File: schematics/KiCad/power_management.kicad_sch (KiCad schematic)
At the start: 52 parts, among them J3 USB_C, Q1 DMG6601LVT-7, Q2 DMG6601LVT-7, Q3 DMG9926UDM, SW4 TL1105SF160R, U4 AP2112K-3.3, U5 MP2615AGQ-Z, U6 BQ29700DSER

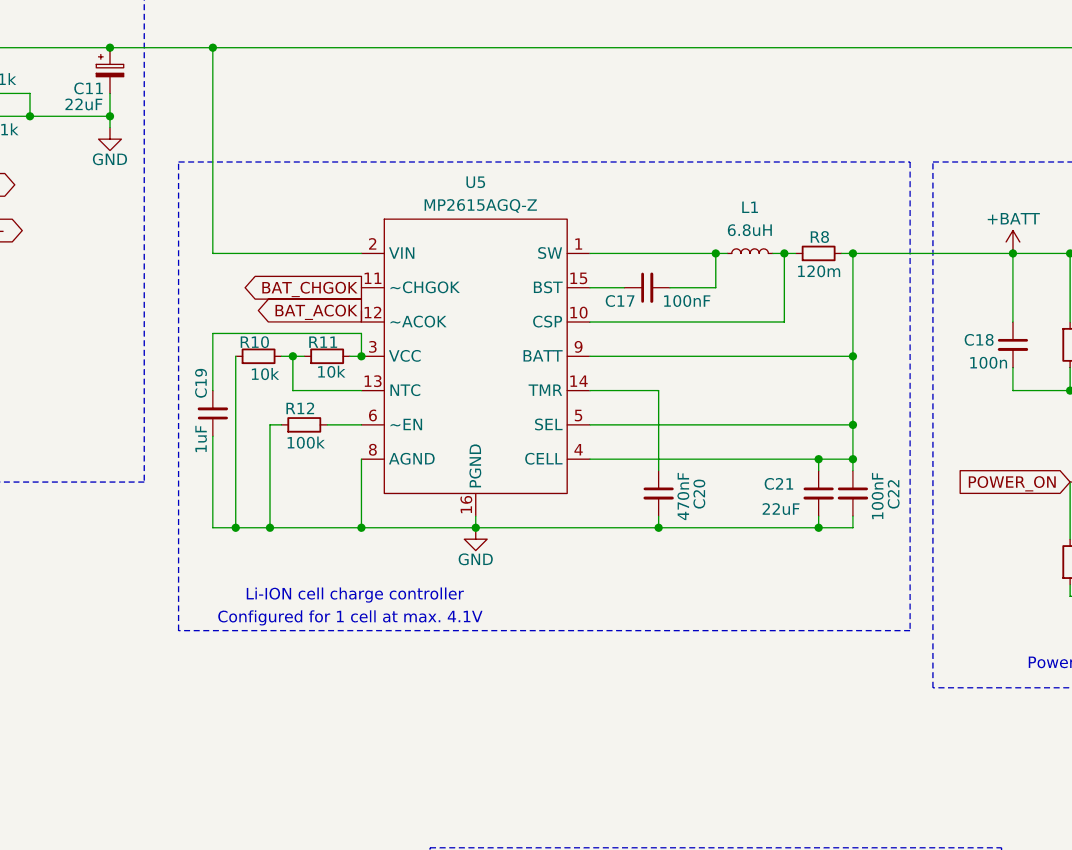
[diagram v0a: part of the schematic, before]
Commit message: re-wire cell selection pins of the charger
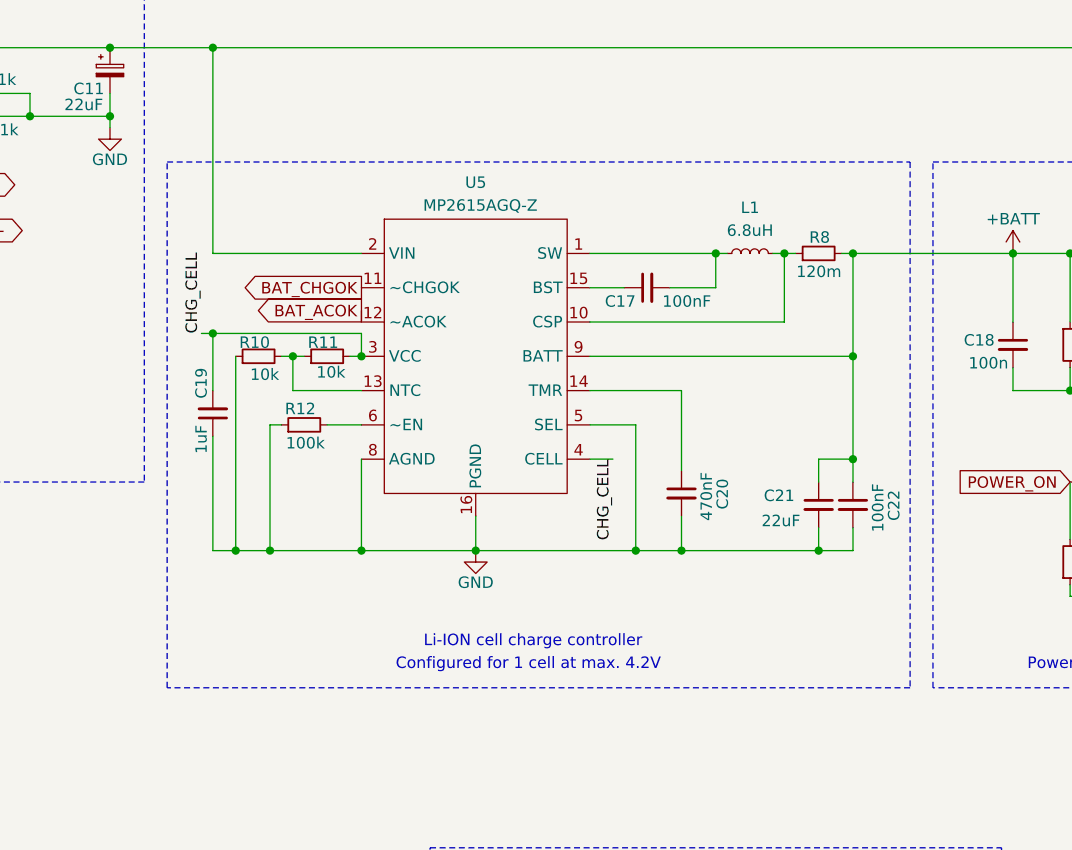
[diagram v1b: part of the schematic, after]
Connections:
- net +BATT: no longer U5.4 (CELL), U5.5 (SEL)
- net GND: now also U5.5 (SEL)
- net CHG_CELL: now reaches C19.2, R11.2, U5.3 (VCC)
- net CHG_CELL: now also U5.4 (CELL)
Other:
- note added: "Configured for 1 cell at max. 4.2V"
- note removed: "Configured for 1 cell at max. 4.1V"
- moved on the sheet: C20, C21, C22

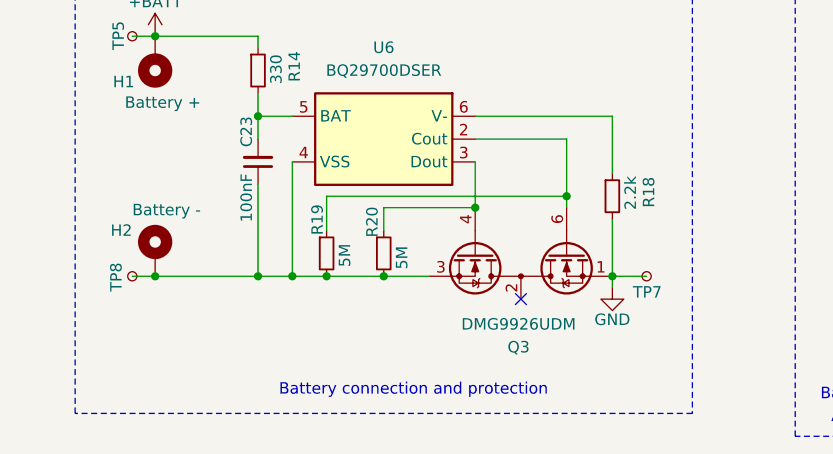
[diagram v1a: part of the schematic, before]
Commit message: re-annotate test points
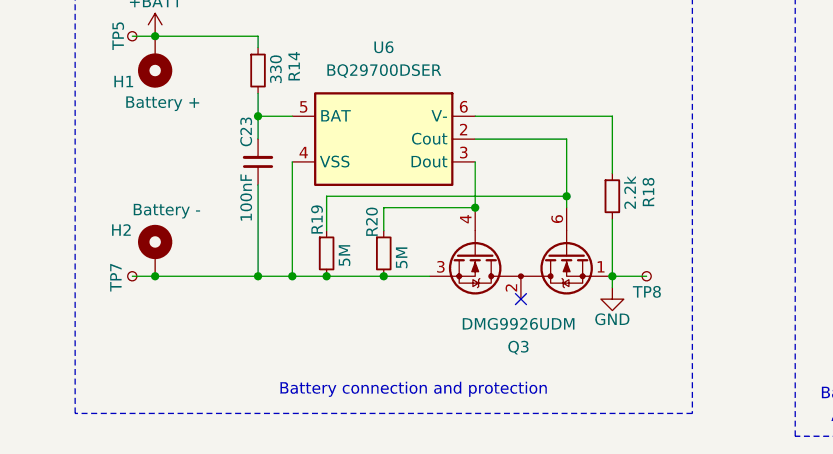
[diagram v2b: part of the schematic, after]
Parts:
- renumbered TP8 to TP7, TP7 to TP8
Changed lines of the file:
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@@
 		(on_board yes)
 		(dnp no)
-		(property "Reference" "TP7"
+		(property "Reference" "TP8"
 			(at 82.296 157.988 90)
 			(effects
@@
 			(project "leany"
 				(path "/e47b2519-93ca-4a48-9414-ecc253dd35f5/702fc064-eab2-4b82-8f62-a654ccd28f72"
-					(reference "TP7")
+					(reference "TP8")
 					(unit 1)
 				)
@@
 		(on_board yes)
 		(dnp no)
-		(property "Reference" "TP8"
+		(property "Reference" "TP7"
 			(at 24.892 154.686 90)
 			(effects
@@
 			(project "leany"
 				(path "/e47b2519-93ca-4a48-9414-ecc253dd35f5/702fc064-eab2-4b82-8f62-a654ccd28f72"
-					(reference "TP8")
-					(unit 1)
-				)
+					(reference "TP7")
+					(unit 1)
+				)

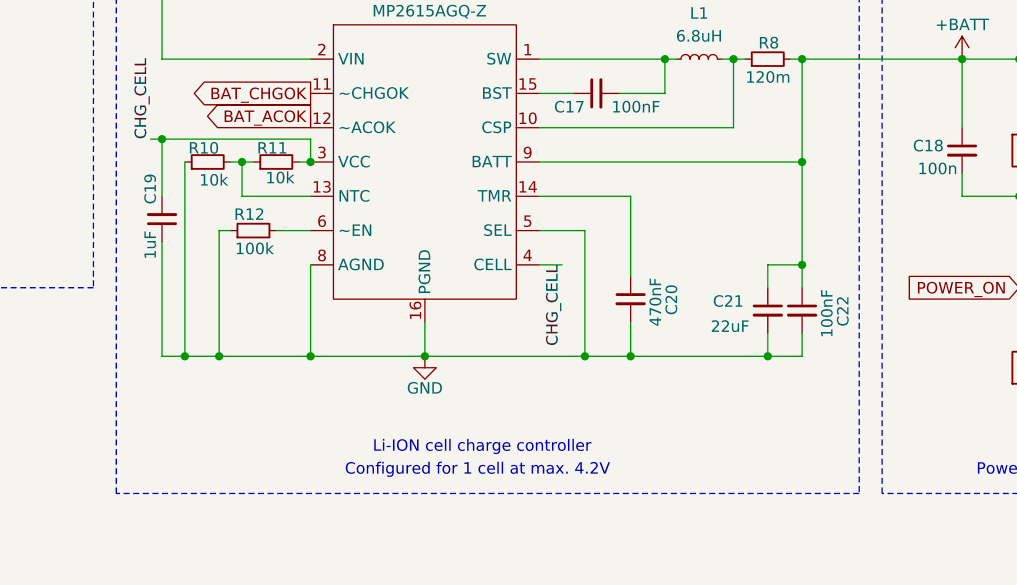
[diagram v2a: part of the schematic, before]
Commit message: change battery decoupling capacitor
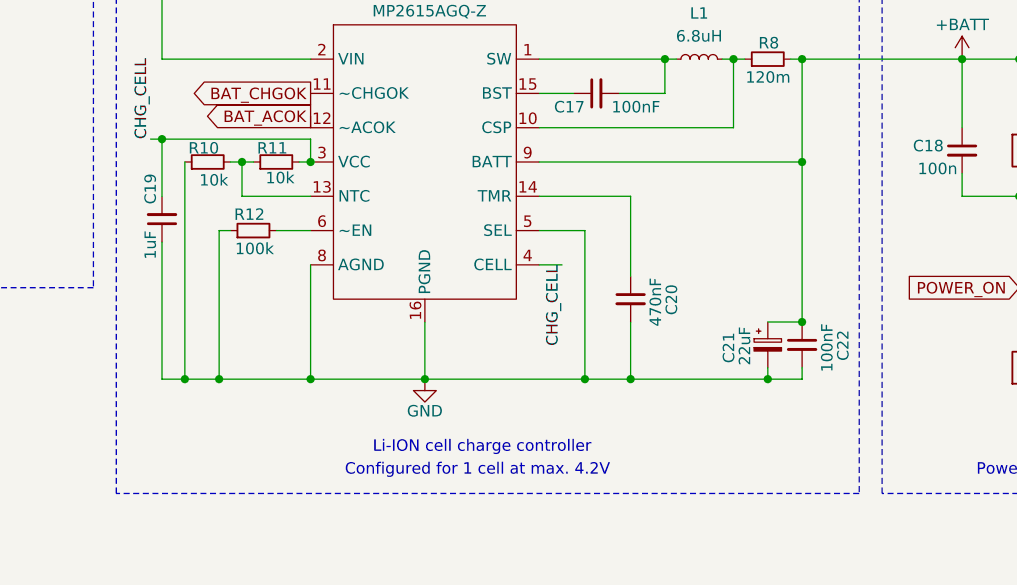
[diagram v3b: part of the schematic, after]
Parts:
- removed C21: 22uF, Capacitor_SMD:C_0201_0603Metric, symbol Device:C_Small
- added C21: 22uF, symbol Device:C_Polarized_Small
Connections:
- net +BATT: now also C21.1
- net GND: now also C21.2
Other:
- moved on the sheet: C22

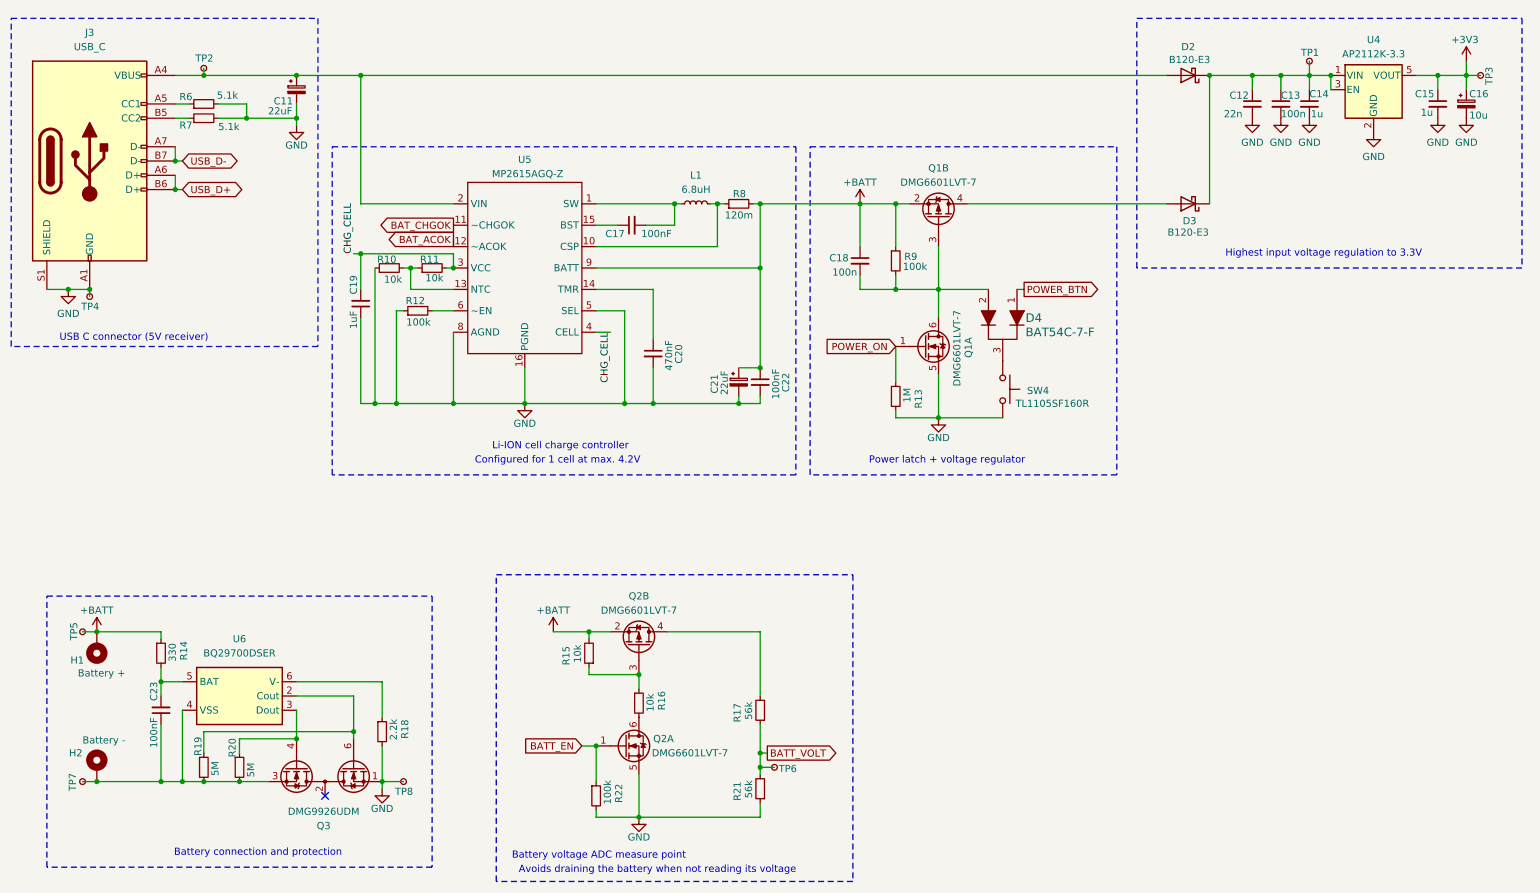
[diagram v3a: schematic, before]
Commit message: assign footprints + add an ideal diode
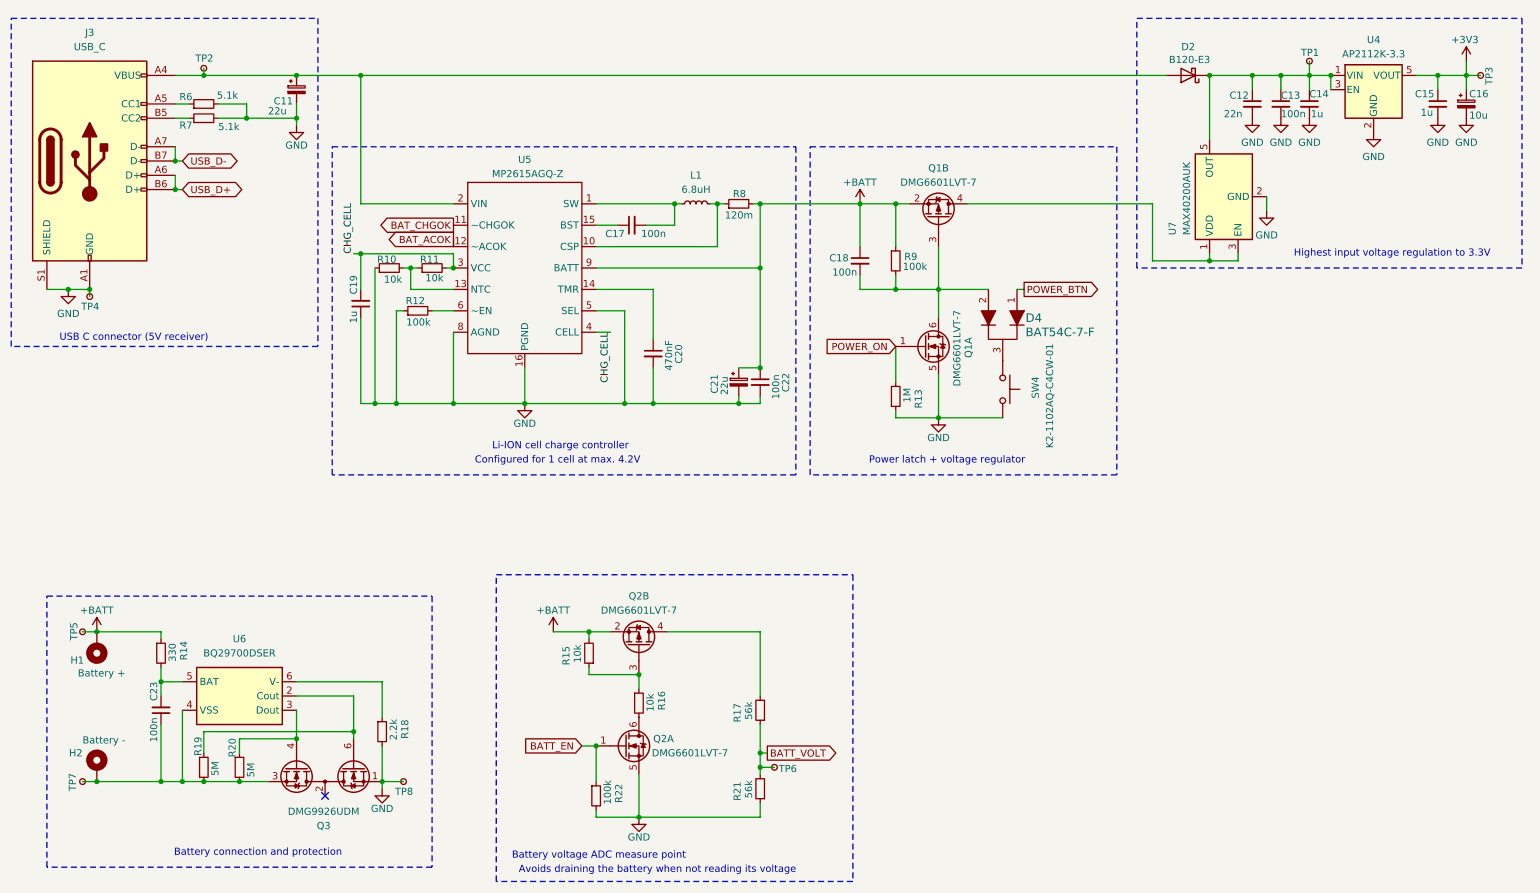
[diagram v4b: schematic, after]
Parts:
- removed D3: B120-E3, Diode_SMD:D_SMA, symbol Diode:B120-E3
- added U7: MAX40200AUK, Package_TO_SOT_SMD:SOT-23-5, symbol Analog_Switch:MAX40200AUK
- C11, C21: value 22uF -> 22u; footprint (none) -> Capacitor_SMD:C_0805_2012Metric
- C12, C13, C14, C15, C18, C20: footprint Capacitor_SMD:C_0201_0603Metric -> Capacitor_SMD:C_0603_1608Metric
- C16: footprint (none) -> Capacitor_SMD:C_0603_1608Metric
- C17, C22, C23: value 100nF -> 100n; footprint Capacitor_SMD:C_0201_0603Metric -> Capacitor_SMD:C_0603_1608Metric
- C19: value 1uF -> 1u; footprint Capacitor_SMD:C_0201_0603Metric -> Capacitor_SMD:C_0603_1608Metric
- D4: footprint digikey-footprints:SOT-23-3 -> Package_TO_SOT_SMD:SOT-23
- SW4: value TL1105SF160R -> K2-1102AQ-C4CW-01; footprint (none) -> Button_Switch_THT:SW_Tactile_SPST_Angled_PTS645Vx31-2LFS
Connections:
- net GND: now also U7.2 (GND)
- net at Q1.4 (D): now also U7.1 (VDD), U7.3 (EN)
- net at C12.1, C13.1, C14.1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: now also U7.5 (OUT)

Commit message: start using a new li-ion charger
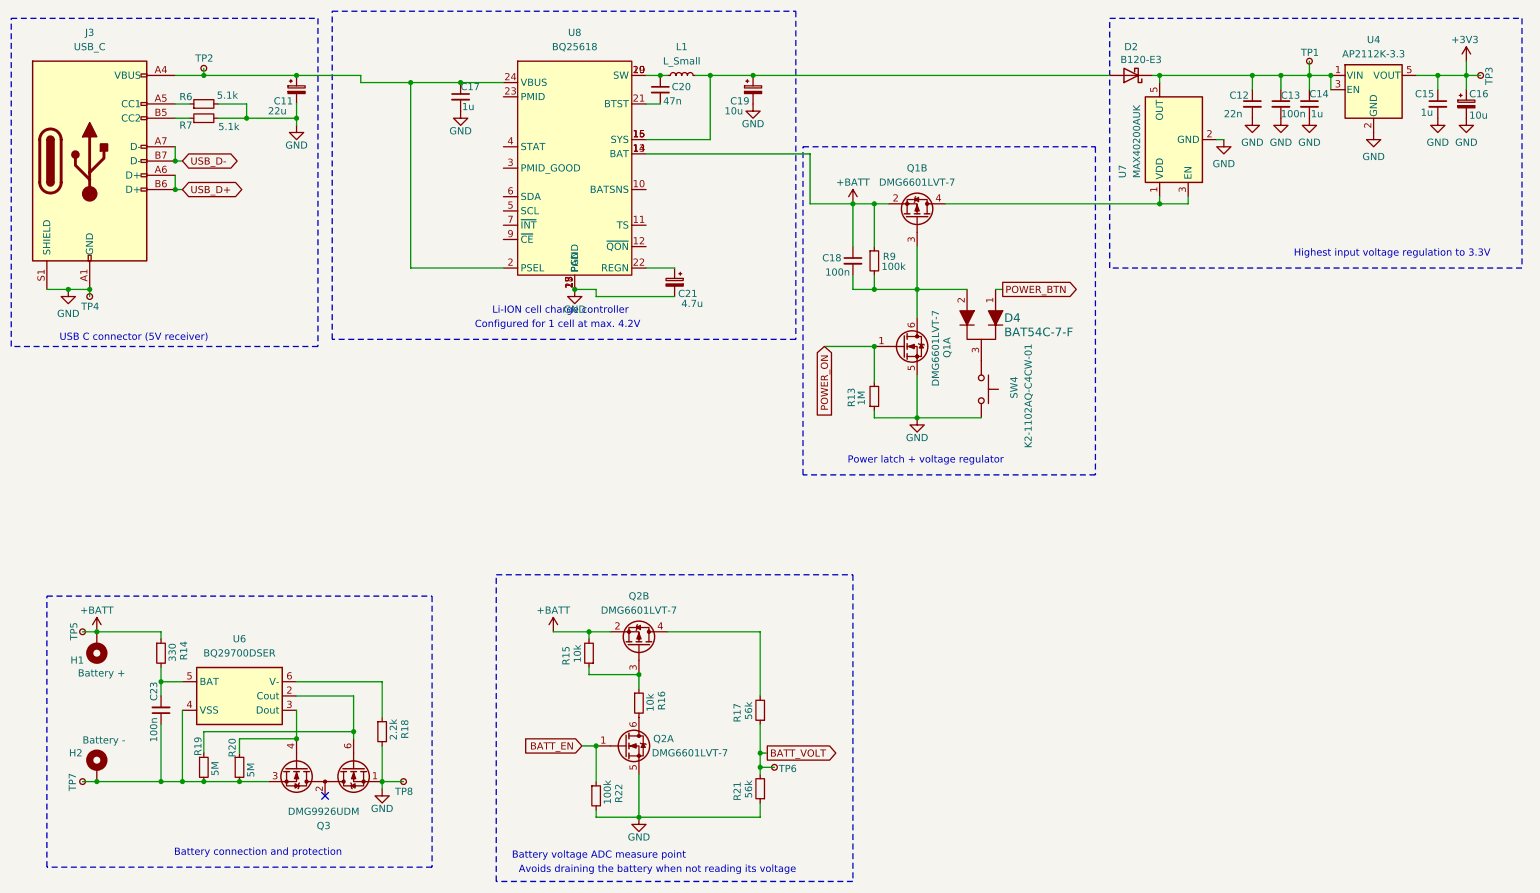
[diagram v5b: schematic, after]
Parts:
- removed C19: 1u, Capacitor_SMD:C_0603_1608Metric, symbol Device:C_Small
- removed C22: 100n, Capacitor_SMD:C_0603_1608Metric, symbol Device:C_Small
- removed R10, R11: 10k, Resistor_SMD:R_0603_1608Metric, symbol Device:R_Small
- removed R12: 100k, Resistor_SMD:R_0603_1608Metric, symbol Device:R_Small
- removed R8: 120m, Resistor_SMD:R_0603_1608Metric, symbol Device:R_Small
- removed U5: MP2615AGQ-Z, symbol leany-symbols:MP2615AGQ-Z
- added C19: 10u, Capacitor_SMD:C_0805_2012Metric, symbol Device:C_Polarized_Small
- added U8: BQ25618, Package_DFN_QFN:Texas_RGE0024H_VQFN-24-1EP_4x4mm_P0.5mm_EP2.7x2.7mm_ThermalVias, symbol leany-symbols:BQ25618
- C17: value 100n -> 1u
- C20: value 470nF -> 47n
- C21: value 22u -> 4.7u
- L1: value 6.8uH -> L_Small
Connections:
- net +BATT: now also U8.13 (BAT), U8.14 (BAT); no longer C21.1
- net GND: now also C17.2, C19.2, U8.17 (PGND), U8.18 (PGND), U8.25 (PAD); no longer C20.2
- net at C11.1, J3.A4 (VBUS), J3.A9 (VBUS)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: now also C17.1, U8.1 (VAC), U8.2 (PSEL), U8.24 (VBUS); no longer D2.2 (A)
- net at L1.1: now also C20.1, U8.19 (SW), U8.20 (SW); no longer C17.2
- net at L1.2: now also D2.2 (A), C19.1, U8.15 (SYS), U8.16 (SYS)
- new net: C21.1, U8.22 (REGN)
- new net: C20.2, U8.21 (BTST)
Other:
- moved on the sheet: C18, D2, D4, Q1A, Q1B, R13, R9, SW4, U7
